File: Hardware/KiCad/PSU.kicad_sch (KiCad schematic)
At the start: 1 part, among them P1 USB_C_Plug_USB2.0

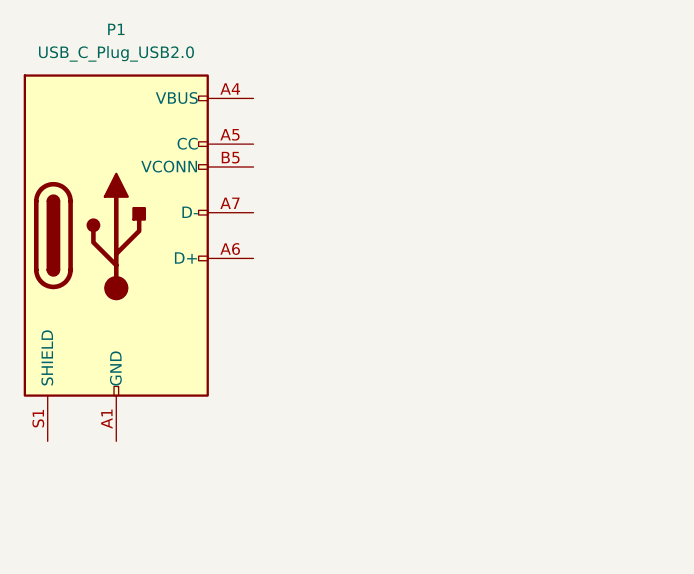
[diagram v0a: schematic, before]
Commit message: Hierarchical sheet for MCU
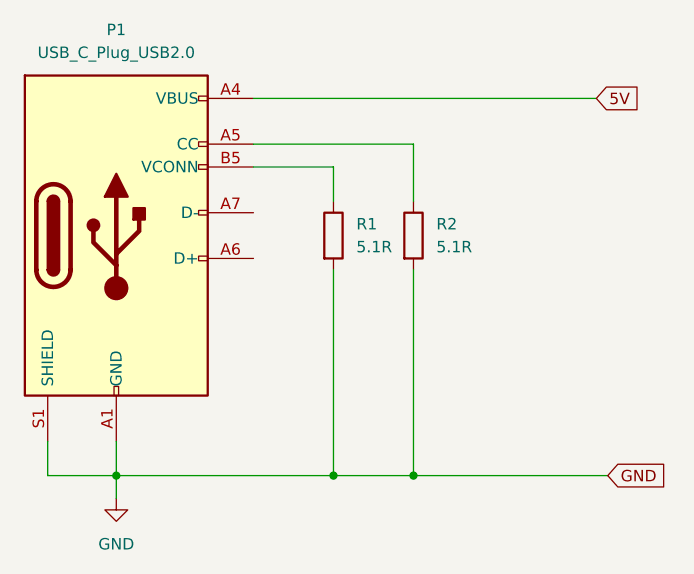
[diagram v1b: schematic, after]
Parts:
- added R1, R2: 5.1R, symbol Device:R
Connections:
- net GND: now reaches P1.A1 (GND), P1.A12 (GND), P1.B1 (GND), P1.B12 (GND)
- net GND: now also P1.S1 (SHIELD), R1.2, R2.2
- net 5V: now reaches P1.A4 (VBUS), P1.A9 (VBUS), P1.B4 (VBUS), P1.B9 (VBUS)
- net at P1.A5 (CC): now also R2.1
- net at P1.B5 (VCONN): now also R1.1

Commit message: Re-orginanisation
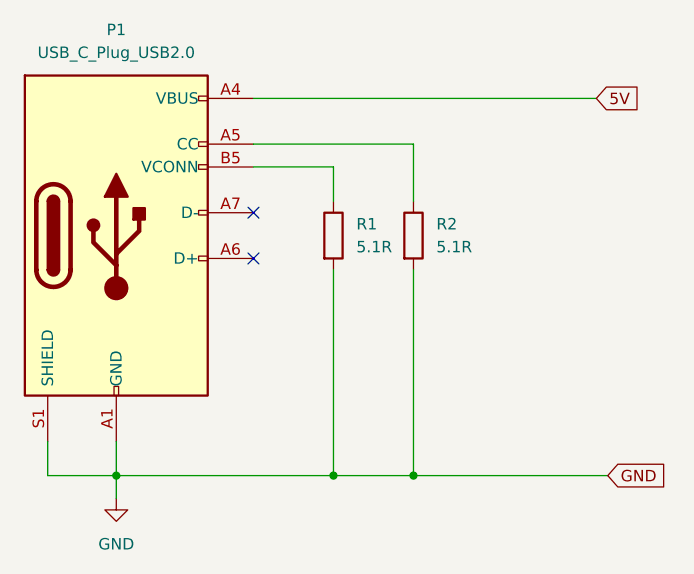
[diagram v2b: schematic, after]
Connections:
- no-connect marks 0 -> 2
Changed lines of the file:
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@@
 (kicad_sch
-	(version 20231120)
+	(version 20250114)
 	(generator "eeschema")
-	(generator_version "8.0")
+	(generator_version "9.0")
 	(paper "A4")
 	(title_block
@@
 		(color 0 0 0 0)
 	)
+	(no_connect
+		(at 90.17 101.6)
+	)
+	(no_connect
+		(at 90.17 96.52)
+	)
 	(wire
